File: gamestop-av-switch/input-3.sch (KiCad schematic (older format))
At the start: 8 parts

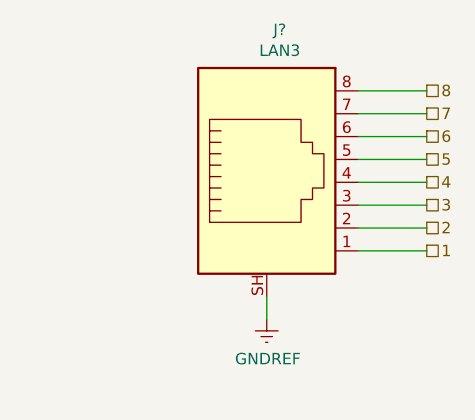
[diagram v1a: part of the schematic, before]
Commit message: Cleaning up extra ethernet pins
Setting no connects on the ports themselves and eliminating the extra
heirarchal labels and pins
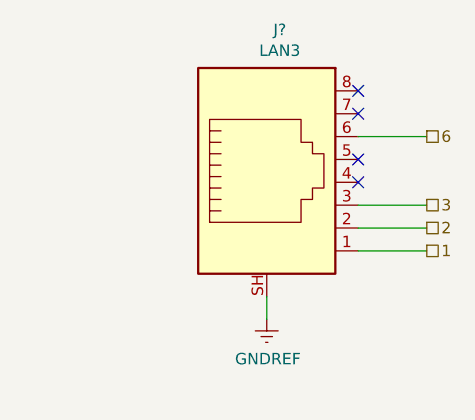
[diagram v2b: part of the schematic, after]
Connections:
- net 4: no longer names the net of J?.4
- net 5: no longer names the net of J?.5
- net 7: no longer names the net of J?.7
- net 8: no longer names the net of J?.8
- no-connect marks 0 -> 4
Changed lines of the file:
@@
 Text HLabel 9850 3350 2    50   UnSpc ~ 0
 3
-Text HLabel 9850 3250 2    50   UnSpc ~ 0
-4
-Text HLabel 9850 3150 2    50   UnSpc ~ 0
-5
 Text HLabel 9850 3050 2    50   UnSpc ~ 0
 6
-Text HLabel 9850 2950 2    50   UnSpc ~ 0
-7
-Text HLabel 9850 2850 2    50   UnSpc ~ 0
-8
-Wire Wire Line
-	9550 2850 9850 2850
-Wire Wire Line
-	9550 2950 9850 2950
 Wire Wire Line
 	9550 3050 9850 3050
-Wire Wire Line
-	9550 3150 9850 3150
-Wire Wire Line
-	9550 3250 9850 3250
 Wire Wire Line
 	9550 3350 9850 3350
@@
 Wire Wire Line
 	9150 3850 9150 3750
+NoConn ~ 9550 2850
+NoConn ~ 9550 2950
+NoConn ~ 9550 3150
+NoConn ~ 9550 3250
 $EndSCHEMATC

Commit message: Annotating and satisfying ERC
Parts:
- gave numbers to parts that had none: 8
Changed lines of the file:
@@
 AR Path="/60F3FEDE/60F9D5E6" Ref="J?"  Part="1"
 AR Path="/60F422FE/60F9D5E6" Ref="J?"  Part="1"
-AR Path="/60F4248B/60F9D5E6" Ref="J?"  Part="1"
-F 0 "J?" H 4850 3125 50  0000 L CNN
+AR Path="/60F4248B/60F9D5E6" Ref="J90"  Part="1"
+F 0 "J90" H 4850 3125 50  0000 L CNN
 F 1 "RD3" H 4850 3034 50  0000 L CNN
 F 2 "" H 4750 3150 50  0001 C CNN
@@
 AR Path="/60F3FEDE/60F9D5EC" Ref="J?"  Part="1"
 AR Path="/60F422FE/60F9D5EC" Ref="J?"  Part="1"
-AR Path="/60F4248B/60F9D5EC" Ref="J?"  Part="1"
-F 0 "J?" H 7150 3767 50  0000 C CNN
+AR Path="/60F4248B/60F9D5EC" Ref="J92"  Part="1"
+F 0 "J92" H 7150 3767 50  0000 C CNN
 F 1 "SV3" H 7150 3676 50  0000 C CNN
 F 2 "" H 7150 3400 50  0001 C CNN
@@
 AR Path="/60F3FEDE/60F9D5F2" Ref="J?"  Part="1"
 AR Path="/60F422FE/60F9D5F2" Ref="J?"  Part="1"
-AR Path="/60F4248B/60F9D5F2" Ref="J?"  Part="1"
-F 0 "J?" H 9207 3917 50  0000 C CNN
+AR Path="/60F4248B/60F9D5F2" Ref="J93"  Part="1"
+F 0 "J93" H 9207 3917 50  0000 C CNN
 F 1 "LAN3" H 9207 3826 50  0000 C CNN
 F 2 "" V 9150 3275 50  0001 C CNN
@@
 AR Path="/60F3FEDE/60F9D5F8" Ref="J?"  Part="1"
 AR Path="/60F422FE/60F9D5F8" Ref="J?"  Part="1"
-AR Path="/60F4248B/60F9D5F8" Ref="J?"  Part="1"
-F 0 "J?" H 4850 3575 50  0000 L CNN
+AR Path="/60F4248B/60F9D5F8" Ref="J91"  Part="1"
+F 0 "J91" H 4850 3575 50  0000 L CNN
 F 1 "G3" H 4850 3484 50  0000 L CNN
 F 2 "" H 4750 3600 50  0001 C CNN
@@
 AR Path="/60F3FEDE/60F9D5FE" Ref="J?"  Part="1"
 AR Path="/60F422FE/60F9D5FE" Ref="J?"  Part="1"
-AR Path="/60F4248B/60F9D5FE" Ref="J?"  Part="1"
-F 0 "J?" H 3600 3125 50  0000 L CNN
+AR Path="/60F4248B/60F9D5FE" Ref="J88"  Part="1"
+F 0 "J88" H 3600 3125 50  0000 L CNN
 F 1 "B3" H 3600 3034 50  0000 L CNN
 F 2 "" H 3500 3150 50  0001 C CNN
@@
 AR Path="/60F3FEDE/60F9D604" Ref="J?"  Part="1"
 AR Path="/60F422FE/60F9D604" Ref="J?"  Part="1"
-AR Path="/60F4248B/60F9D604" Ref="J?"  Part="1"
-F 0 "J?" H 3600 3575 50  0000 L CNN
+AR Path="/60F4248B/60F9D604" Ref="J89"  Part="1"
+F 0 "J89" H 3600 3575 50  0000 L CNN
 F 1 "Y3" H 3600 3484 50  0000 L CNN
 F 2 "" H 3500 3600 50  0001 C CNN
@@
 AR Path="/60F3FEDE/60F9D60A" Ref="J?"  Part="1"
 AR Path="/60F422FE/60F9D60A" Ref="J?"  Part="1"
-AR Path="/60F4248B/60F9D60A" Ref="J?"  Part="1"
-F 0 "J?" H 2500 3125 50  0000 L CNN
+AR Path="/60F4248B/60F9D60A" Ref="J86"  Part="1"
+F 0 "J86" H 2500 3125 50  0000 L CNN
 F 1 "R3" H 2500 3034 50  0000 L CNN
 F 2 "" H 2400 3150 50  0001 C CNN
@@
 AR Path="/60F3FEDE/60F9D610" Ref="J?"  Part="1"
 AR Path="/60F422FE/60F9D610" Ref="J?"  Part="1"
-AR Path="/60F4248B/60F9D610" Ref="J?"  Part="1"
-F 0 "J?" H 2500 3575 50  0000 L CNN
+AR Path="/60F4248B/60F9D610" Ref="J87"  Part="1"
+F 0 "J87" H 2500 3575 50  0000 L CNN
 F 1 "L3" H 2500 3484 50  0000 L CNN
 F 2 "" H 2400 3600 50  0001 C CNN
@@
 C
 $Comp
-L power:GNDREF #PWR?
+L power:GNDREF #PWR08
 U 1 1 60F9D61D
 P 5150 4100
-F 0 "#PWR?" H 5150 3850 50  0001 C CNN
+F 0 "#PWR08" H 5150 3850 50  0001 C CNN
 F 1 "GNDREF" H 5155 3927 50  0000 C CNN
 F 2 "" H 5150 4100 50  0001 C CNN
@@
 Connection ~ 7150 3800
 $Comp
-L power:GNDREF #PWR?
+L power:GNDREF #PWR09
 U 1 1 60F9D647
 P 6750 3950
-F 0 "#PWR?" H 6750 3700 50  0001 C CNN
+F 0 "#PWR09" H 6750 3700 50  0001 C CNN
 F 1 "GNDREF" H 6755 3777 50  0000 C CNN
 F 2 "" H 6750 3950 50  0001 C CNN
@@
 	9550 3550 9850 3550
 $Comp
-L power:GNDREF #PWR?
+L power:GNDREF #PWR010
 U 1 1 60F9D65F
 P 9150 3850
-F 0 "#PWR?" H 9150 3600 50  0001 C CNN
+F 0 "#PWR010" H 9150 3600 50  0001 C CNN
 F 1 "GNDREF" H 9155 3677 50  0000 C CNN
 F 2 "" H 9150 3850 50  0001 C CNN
